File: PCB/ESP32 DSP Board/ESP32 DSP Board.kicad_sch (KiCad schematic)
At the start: 4 parts

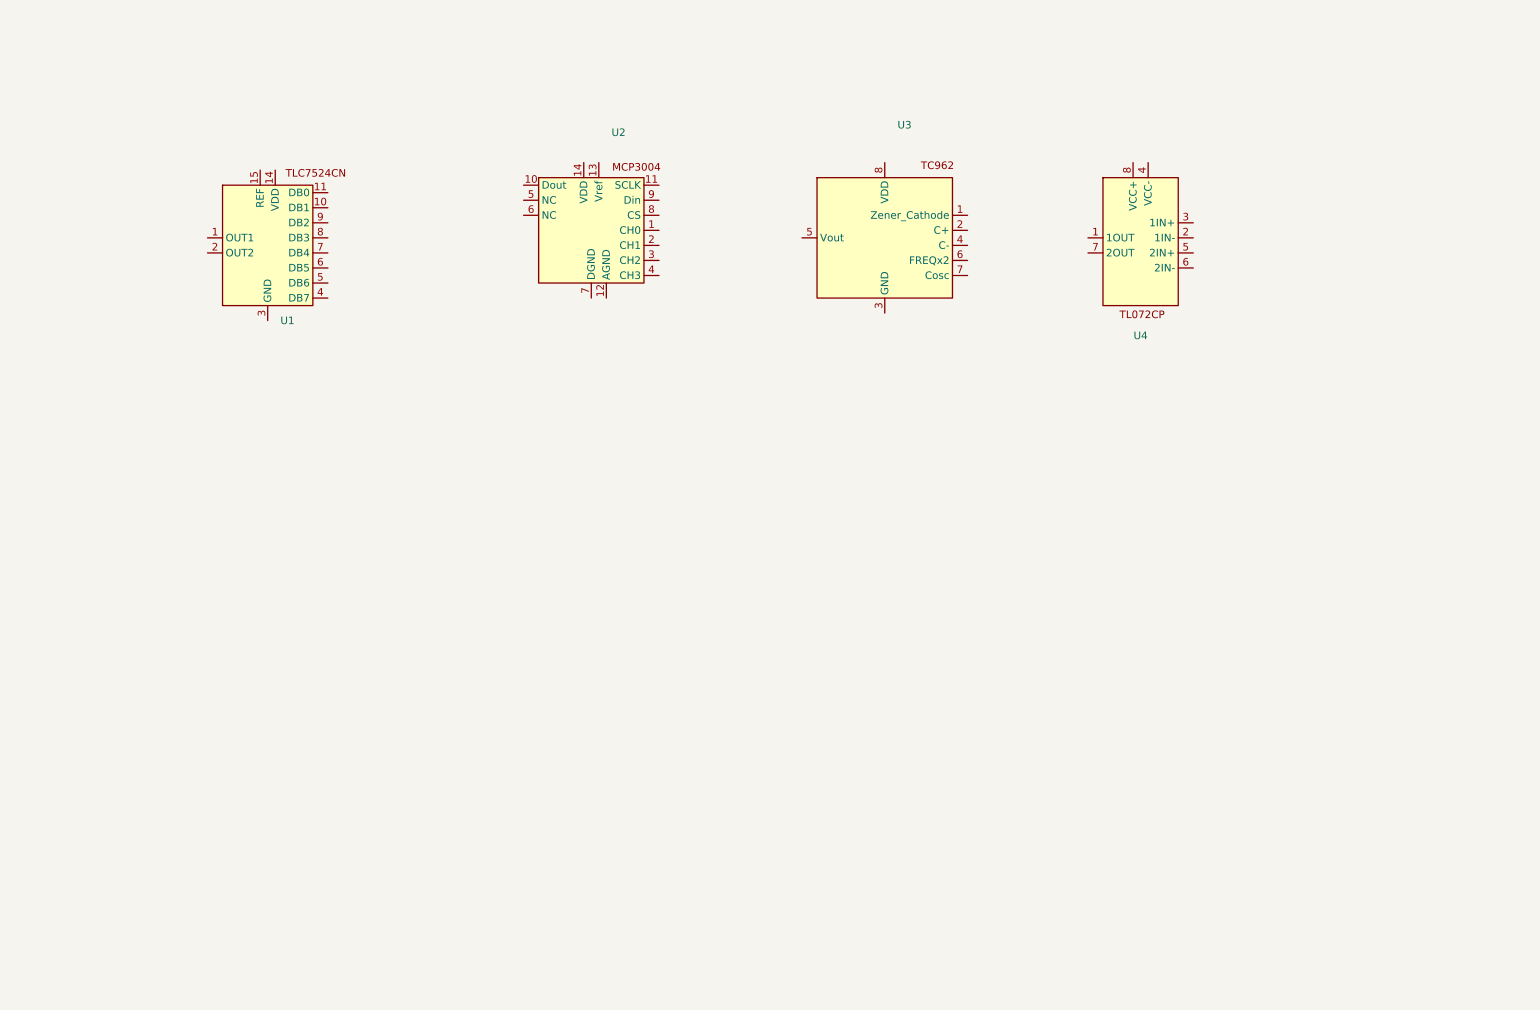
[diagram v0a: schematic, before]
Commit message: Schematic updates
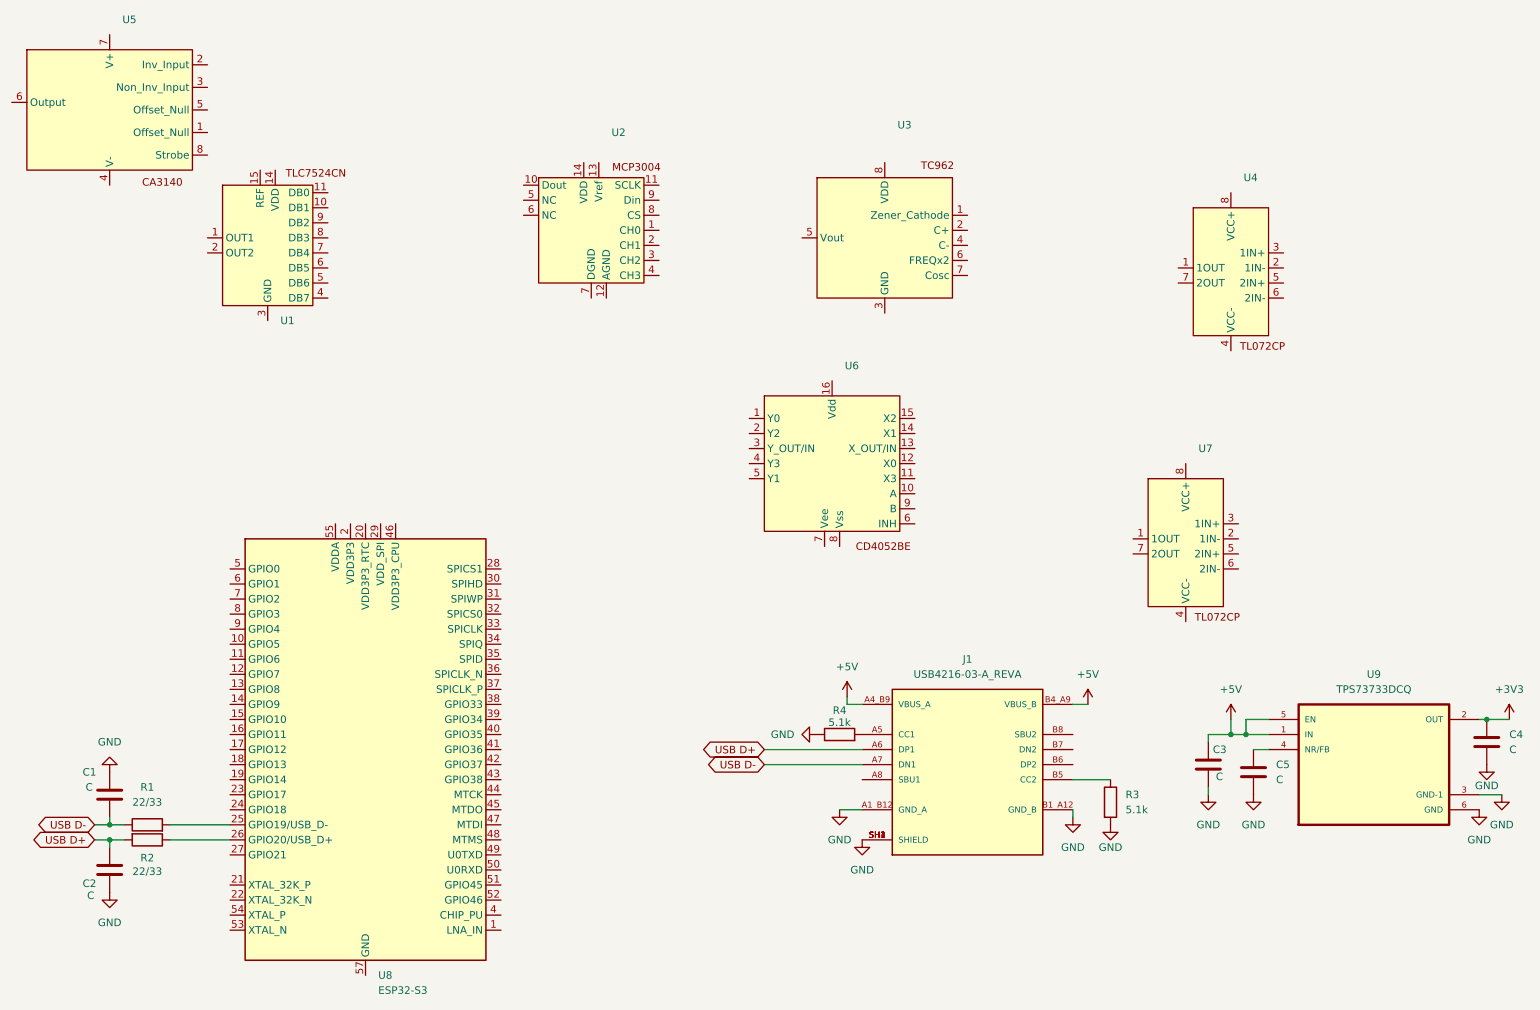
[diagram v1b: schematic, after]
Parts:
- added C1, C2, C3, C4, C5: C, symbol Device:C
- added J1: USB4216-03-A_REVA, USB4216-03-A_REVA:GCT_USB4216-03-A_REVA, symbol USB4216-03-A_REVA:USB4216-03-A_REVA
- added R1, R2: 22/33, symbol Device:R
- added R3, R4: 5.1k, symbol Device:R
- added U5: ~, symbol Amplifier_Operational_Renesas:CA3140A
- added U6: ~, symbol Mux_Demux_TI:CD4052BE
- added U7: ~, symbol Amplifier_Operational_TI:TL072CP
- added U8: ESP32-S3, Package_DFN_QFN:QFN-56-1EP_7x7mm_P0.4mm_EP4x4mm, symbol MCU_Espressif:ESP32-S3
- added U9: TPS73733DCQ, TPS73733DCQ:SOT127P706X180-6N, symbol TPS73733DCQ:TPS73733DCQ
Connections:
- new net: C5.1, U9.4 (NR/FB)
- new net: R2.1, U8.26 (GPIO20/USB_D+)
- new net: U8.2 (VDD3P3), U8.3 (VDD3P3)
- new net: R1.2, U8.25 (GPIO19/USB_D-)
- new net: U8.55 (VDDA), U8.56 (VDDA)
- new net: J1.B5 (CC2), R3.1
- new net: J1.A5 (CC1), R4.2
- new net +3V3: C4.1, U9.2 (OUT)
- new net +5V: C3.1, J1.A4_B9 (VBUS_A), J1.B4_A9 (VBUS_B), U9.1 (IN), U9.5 (EN)
- new net GND: C1.1, C2.2, C3.2, C4.2, C5.2, J1.A1_B12 (GND_A), J1.B1_A12 (GND_B), J1.SH1 (SHIELD), J1.SH2 (SHIELD), J1.SH3 (SHIELD), J1.SH4 (SHIELD), R3.2, R4.1, U9.3 (GND-1), U9.6 (GND)
- new net USB D+: C2.1, J1.A6 (DP1), R2.2
- new net USB D-: C1.2, J1.A7 (DN1), R1.1

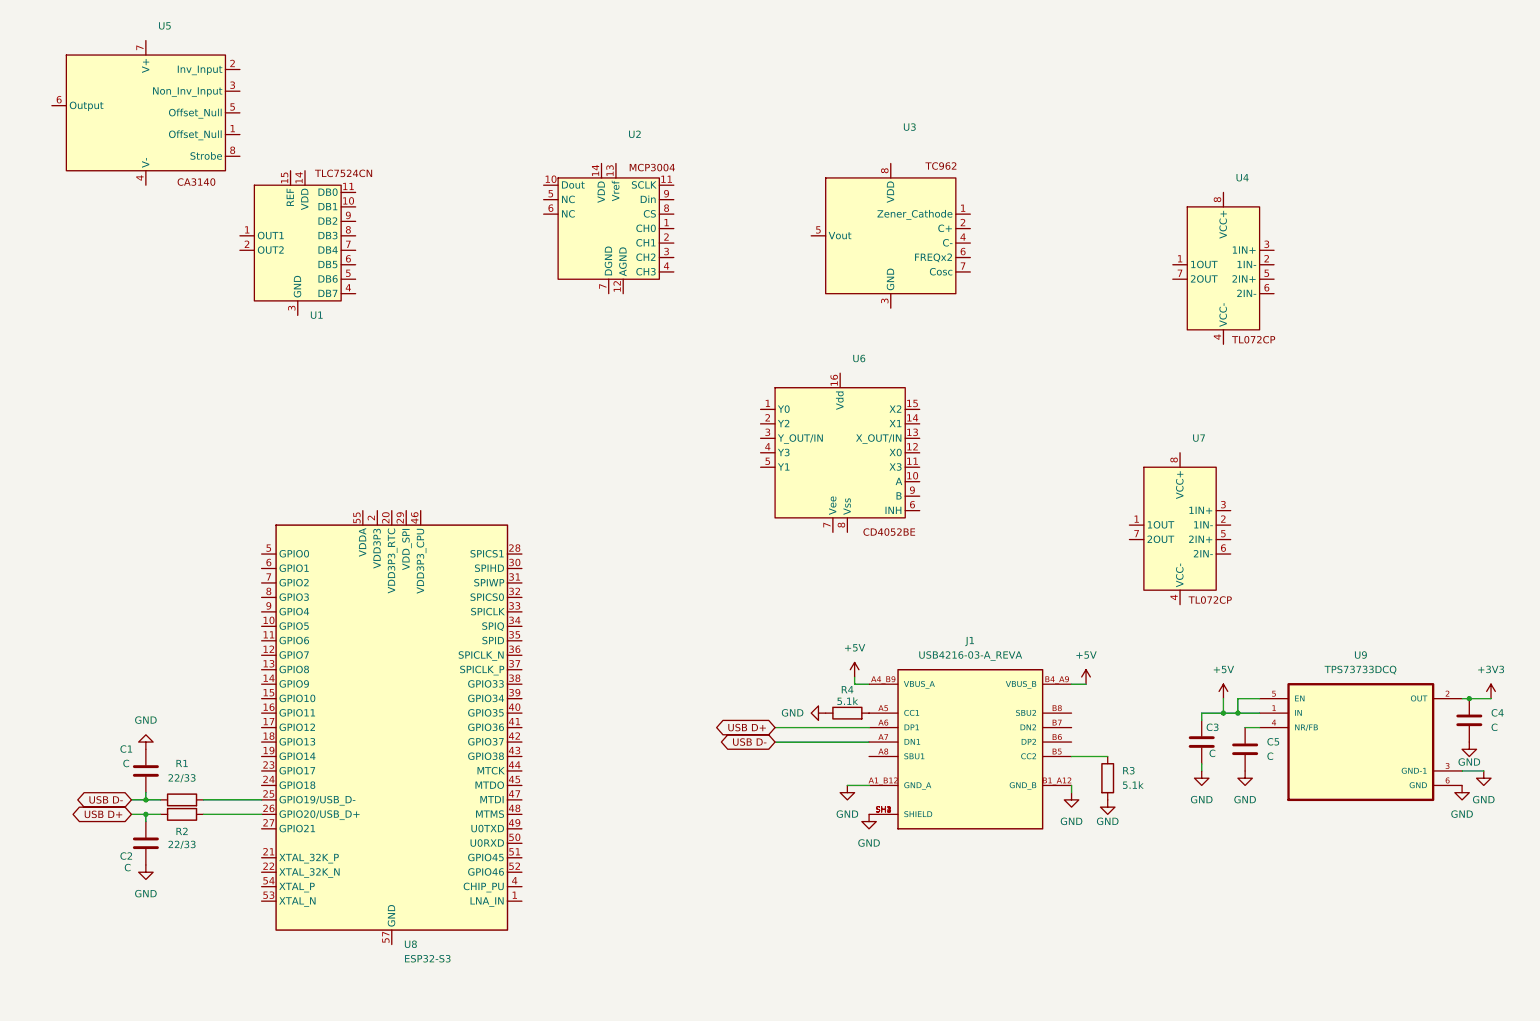
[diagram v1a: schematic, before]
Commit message: Schematic updates
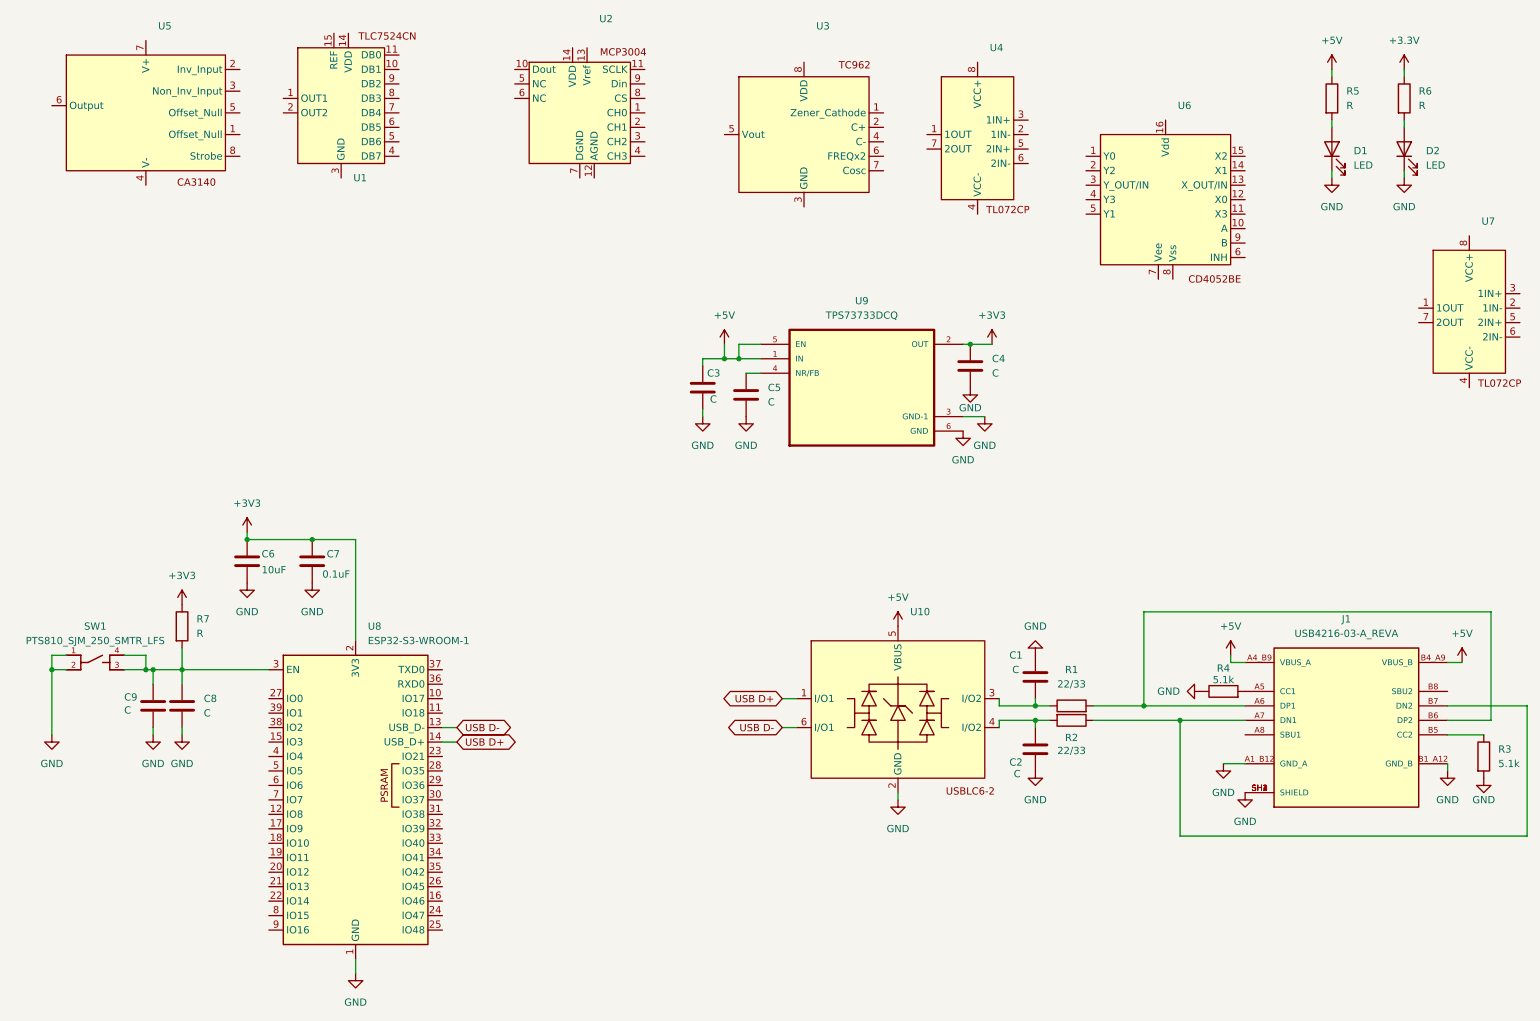
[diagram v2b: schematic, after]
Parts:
- removed U8: ESP32-S3, Package_DFN_QFN:QFN-56-1EP_7x7mm_P0.4mm_EP4x4mm, symbol MCU_Espressif:ESP32-S3
- added C6: 10uF, symbol Device:C
- added C7: 0.1uF, symbol Device:C
- added C8, C9: C, symbol Device:C
- added D1, D2: LED, symbol Device:LED
- added R5, R6, R7: R, symbol Device:R
- added SW1: PTS810_SJM_250_SMTR_LFS, PTS810_SJM_250_SMTR_LFS:SW_PTS810_SJM_250_SMTR_LFS, symbol PTS810_SJM_250_SMTR_LFS:PTS810_SJM_250_SMTR_LFS
- added U10: ~, symbol ESD_Protection_STM:USBLC-2
- added U8: ESP32-S3-WROOM-1, RF_Module:ESP32-S3-WROOM-1, symbol RF_Module:ESP32-S3-WROOM-1
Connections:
- net +3V3: now also C6.1, C7.1, R7.1, U8.2 (3V3)
- net +5V: now also R5.1, U10.5 (VBUS)
- net GND: now also C6.2, C7.2, C8.2, C9.2, D1.1 (K), D2.1 (K), SW1.1, SW1.2, U10.2 (GND), U8.1 (GND), U8.40 (GND), U8.41 (GND)
- net USB D+: now also U10.1 (I/O1), U8.14 (USB_D+); no longer C2.1, J1.A6 (DP1), R2.2
- net USB D-: now also U10.6 (I/O1), U8.13 (USB_D-); no longer C1.2, J1.A7 (DN1), R1.1
- net at R2.1: now also J1.A7 (DN1), J1.B7 (DN2)
- net at R1.2: now also J1.A6 (DP1), J1.B6 (DP2)
- new net: C2.1, R2.2, U10.4 (I/O2)
- new net: C8.1, C9.1, R7.2, SW1.3, SW1.4, U8.3 (EN)
- new net: C1.2, R1.1, U10.3 (I/O2)
- new net: D2.2 (A), R6.2
- new net: D1.2 (A), R5.2
- new net +3.3V: R6.1
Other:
- moved on the sheet: C1, C2, C3, C4, C5, J1, R1, R2, R3, R4, U1, U2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

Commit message: Schematic updates, added USB-UART bridge and tC962
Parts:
- added C10, C11, C13, C14, C16: C, symbol Device:C
- added C12, C15: 10uF, symbol Device:C
- added D3: LED, symbol Device:LED
- added J2: USB4216-03-A_REVA, USB4216-03-A_REVA:GCT_USB4216-03-A_REVA, symbol USB4216-03-A_REVA:USB4216-03-A_REVA
- added R10, R11: 5.1k, symbol Device:R
- added R12: 1K, symbol Device:R
- added R13, R14: R, symbol Device:R
- added R15: 470, symbol Device:R
- added R16: 220, symbol Device:R
- added R8, R9: 22/33, symbol Device:R
- added U11: INTERFACE-CP2102-GMR_QFN28_, INTERFACE-CP2102-GMR_QFN28_:QFN28G_0.5-5X5MM, symbol INTERFACE-CP2102-GMR_QFN28_:INTERFACE-CP2102-GMR_QFN28_
- added U12: ~, symbol ESD_Protection_STM:USBLC-2
- R5, R6: value R -> 1K
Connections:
- net +3.3V: now also R12.2
- net +3V3: now also U2.13 (Vref), C12.1, C14.1, U11.6 (VDD)
- net +5V: now also U2.14 (VDD), U3.8 (VDD), U4.8 (VCC+), C13.1, J2.A4_B9 (VBUS_A), J2.B4_A9 (VBUS_B), R16.2, U11.8 (VBUS), U12.5 (VBUS)
- net GND: now also U2.12 (AGND), U2.7 (DGND), U3.3 (GND), C10.1, C11.2, C12.2, C13.2, C14.2, C15.2, D3.1 (K), J2.A1_B12 (GND_A), J2.B1_A12 (GND_B), J2.SH1 (SHIELD), J2.SH2 (SHIELD), J2.SH3 (SHIELD), J2.SH4 (SHIELD), R10.1, R11.2, R13.2, U11.29 (GND@1), U12.2 (GND)
- net ADC CH0: now reaches U2.1 (CH0)
- net ADC Dout: now reaches U2.10 (Dout)
- net ADC SCLK: now reaches U2.11 (SCLK)
- net ADC CH1: now reaches U2.2 (CH1)
- net ADC CH2: now reaches U2.3 (CH2)
- net ADC CH3: now reaches U2.4 (CH3)
- net ADC CS: now reaches U2.8 (CS)
- net ADC Din: now reaches U2.9 (Din)
- net at U8.21 (IO13): now also R14.2
- net ESP Rx: now reaches U8.36 (RXD0)
- net ESP Rx: now also U11.26 (TXD)
- net ESP Tx: now reaches U8.37 (TXD0)
- net ESP Tx: now also U11.25 (RXD)
- net -5V: now reaches U4.4 (VCC-)
- net -5V: now also U3.5 (Vout), C15.1
- net at U3.1 (Zener_Cathode): now also R15.1
- net at U3.2 (C+): now also C16.2
- net at U3.4 (C-): now also C16.1
- new net: R12.1, U11.9 (~{RST})
- new net: C10.2, R8.1, U12.3 (I/O2)
- new net: J2.A6 (DP1), J2.B6 (DP2), R8.2
- new net: J2.A5 (CC1), R10.2
- new net: R13.1, U11.11 (~{SUSPEND})
- new net: U11.4 (D+), U12.1 (I/O1)
- new net: U11.5 (D-), U12.6 (I/O1)
- new net: C11.1, R9.2, U12.4 (I/O2)
- new net: J2.B5 (CC2), R11.1
- new net: D3.2 (A), R14.1
- new net: J2.A7 (DN1), J2.B7 (DN2), R9.1
- new net: R15.2, R16.1
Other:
- moved on the sheet: C1, C2, C3, C4, C5, C6, C7, C8, C9, D1, D2, J1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

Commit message: Schematic updates, ADC, DAC, and amplifiers
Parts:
- added C17: 100p, symbol Device:C
- added C18: C, symbol Device:C
- added D4: LED, symbol Device:LED
- added R17, R18, R20, R21, R22, R23, R27: R, symbol Device:R
- added R19: 10K, symbol Device:R
- added R24, R25, R26: 22K, symbol Device:R
- added R28: 1K, symbol Device:R
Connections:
- net ADC CH0 is gone; now on an unnamed net: U2.1 (CH0)
- net +5V: now also U1.14 (VDD)
- net GND: now also U1.1 (OUT1), U1.2 (OUT2), U1.3 (GND), U5.4 (V-), U6.6 (INH), U6.7 (Vee), U6.8 (Vss), U7.4 (VCC-), C17.2, D4.1 (K), R19.1, R24.2, R26.2
- net at U5.2 (Inv_Input): now also U6.3 (Y_OUT/IN), R19.2
- net DAC OUT: now reaches U5.3 (Non_Inv_Input)
- net DAC OUT: now also U1.15 (REF)
- net CH0 OUT: now reaches U5.6 (Output)
- net CH0 OUT: now also R20.1, R21.1, R22.1, R23.1
- net VDD: now reaches U5.7 (V+)
- net VDD: now also U6.16 (Vdd), U7.8 (VCC+), R28.1
- net at U4.1 (1OUT): now also C18.2
- net at U4.3 (1IN+): now also C17.1, R18.1
- net 2A: now reaches U7.1 (1OUT)
- net 2A: now also U6.10 (A), R27.1
- net at U7.2 (1IN-): now also R26.1, R27.2
- net A: now reaches U7.3 (1IN+)
- net B: now reaches U7.5 (2IN+)
- net 2B: now reaches U7.6 (2IN-)
- net 2B: now also U6.9 (B), R24.1, R25.1
- net at U7.7 (2OUT): now also R25.2
- net DB1: now reaches U1.10 (DB1)
- net DB0: now reaches U1.11 (DB0)
- net DB7: now reaches U1.4 (DB7)
- net DB6: now reaches U1.5 (DB6)
- net DB5: now reaches U1.6 (DB5)
- net DB4: now reaches U1.7 (DB4)
- net DB3: now reaches U1.8 (DB3)
- net DB2: now reaches U1.9 (DB2)
- net Y0: now reaches U6.1 (Y0)
- net Y0: now also R20.2
- net Y2: now reaches U6.2 (Y2)
- net Y2: now also R22.2
- net Y3: now reaches U6.4 (Y3)
- net Y3: now also R23.2
- net Y1: now reaches U6.5 (Y1)
- net Y1: now also R21.2
- new net: D4.2 (A), R28.2
- new net: C18.1, R17.1, R18.2
- new net A0: R17.2
- new net CS': U1.12 (CS')
- new net WR': U1.13 (WR')
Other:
- moved on the sheet: C13, C14, C15, C16, C3, C4, C5, D1, D2, R15, R16, R5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

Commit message: Schematic first rev complete
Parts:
- removed C8: C, symbol Device:C
- added C19: 0.1uF, symbol Device:C
- added C20, C21: 100p, symbol Device:C
- added J3: ~, symbol Terminal_Block_Generic:4-Way-Screw-Block
- added J4, J5: ~, symbol Terminal_Block_Generic:2-Way-Screw-Block
- added J6: ~, symbol Pin_Header_Generic:16_Pin_Header
- added J7: ~, symbol Pin_Header_Generic:4_Pin_Header
- added R29: 10K, symbol Device:R
- added R30, R31: 2K, symbol Device:R
- added SW2: PTS810_SJM_250_SMTR_LFS, PTS810_SJM_250_SMTR_LFS:SW_PTS810_SJM_250_SMTR_LFS, symbol PTS810_SJM_250_SMTR_LFS:PTS810_SJM_250_SMTR_LFS
- C1, C10, C11, C2, C9: value C -> 0.1uF
- C18: value C -> 100p
- C3, C4, C5: value C -> 1uF
- R13, R14: value R -> 1K
- R17, R18: value R -> 2K
- R27: value R -> 22K
- R7: value R -> 10K
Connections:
- net +3.3V: now also J7.2
- net +3V3: now also R29.1
- net +5V: now also J7.1
- net A: now also U8.22 (IO14)
- net ADC CH1: now also J3.2, R30.2; no longer U2.2 (CH1)
- net ADC CH2: now also J3.3
- net ADC CH3: now also J3.4
- net ADC CS: now also U8.25 (IO48)
- net ADC Din: now also U8.24 (IO47)
- net ADC Dout: now also U8.23 (IO21)
- net ADC SCLK: now also U8.26 (IO45)
- net B: now also U8.21 (IO13)
- net CS': now also U8.38 (IO2)
- net DAC OUT: now also J5.1
- net DB0: now also U8.28 (IO35)
- net DB1: now also U8.29 (IO36)
- net DB2: now also U8.30 (IO37)
- net DB3: now also U8.31 (IO38)
- net DB4: now also U8.32 (IO39)
- net DB5: now also U8.33 (IO40)
- net DB6: now also U8.34 (IO41)
- net DB7: now also U8.35 (IO42)
- net GND: now also U11.3 (GND), C19.2, C21.2, J4.2, J5.2, J6.16, J7.3, J7.4, SW2.1, SW2.2
- net VDD: now also J4.1
- net WR': now also U8.39 (IO1)
- net IO17: now reaches U8.10 (IO17)
- net IO17: now also J6.7
- net IO18: now reaches U8.11 (IO18)
- net IO18: now also J6.8
- net IO8: now reaches U8.12 (IO8)
- net IO8: now also J6.9
- net IO3: now reaches U8.15 (IO3)
- net IO3: now also J6.10
- net IO46: now reaches U8.16 (IO46)
- net IO46: now also J6.11
- net IO9: now reaches U8.17 (IO9)
- net IO9: now also J6.12
- net IO10: now reaches U8.18 (IO10)
- net IO10: now also J6.13
- net IO11: now reaches U8.19 (IO11)
- net IO11: now also J6.14
- net IO12: now reaches U8.20 (IO12)
- net IO12: now also J6.15
- net at R14.2: now also U8.9 (IO16); no longer U8.21 (IO13)
- net BOOT: now reaches U8.27 (IO0)
- net BOOT: now also C19.1, R29.2, SW2.3, SW2.4
- net IO4: now reaches U8.4 (IO4)
- net IO4: now also J6.1
- net IO5: now reaches U8.5 (IO5)
- net IO5: now also J6.2
- net IO6: now reaches U8.6 (IO6)
- net IO6: now also J6.3
- net IO7: now reaches U8.7 (IO7)
- net IO7: now also J6.4
- net at U4.6 (2IN-): now also C21.1, R31.1
- net at U4.7 (2OUT): now also U2.2 (CH1), C20.2
- net A0 renamed ADC CH0
- net ADC CH0: now also J3.1
- new net: C20.1, R30.1, R31.2
- new net IO15: J6.5
- new net IO16: J6.6
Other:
- note added: "ADC, DAC and input filter"
- note added: "ESP32"
- note added: "Gain Amplifier"
- note added: "USB, 5V & 3V3 Supply"
- note added: "USB-UART Bridge"
- moved on the sheet: C1, C10, C11, C12, C13, C14, C15, C16, C17, C18, C2, C3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
